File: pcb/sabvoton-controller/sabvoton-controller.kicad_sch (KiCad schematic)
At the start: 26 parts, among them J1 Conn_02x03_Counter_Clockwise, J2 Conn_01x30, U1 ESP32-WROOM-32, U2 XL7015E1, U3 XL7015E1

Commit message: Added 1.8V converter (voltage reference)
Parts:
- added U?: LM1117-1.8, Package_TO_SOT_SMD:SOT-223-3_TabPin2, symbol Regulator_Linear:LM1117-1.8
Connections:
- net 3.3V: now also U?.3 (VI)
- net GND: now also U?.1 (GND)
- new net 1.8V: U?.2 (VO)
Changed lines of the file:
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@@
+    (stroke (width 0) (type default) (color 0 0 0 0))
+  )
+  (wire (pts (xy 572.77 82.55) (xy 579.12 82.55))
     (stroke (width 0) (type default) (color 0 0 0 0))
   )
@@
     (stroke (width 0) (type default) (color 0 0 0 0))
   )
+  (wire (pts (xy 586.74 91.44) (xy 586.74 90.17))
+    (stroke (width 0) (type default) (color 0 0 0 0))
+  )
   (wire (pts (xy 504.19 77.47) (xy 504.19 67.31))
     (stroke (width 0) (type default) (color 0 0 0 0))
   )
+  (wire (pts (xy 571.5 91.44) (xy 586.74 91.44))
+    (stroke (width 0) (type default) (color 0 0 0 0))
+  )
   (wire (pts (xy 506.73 74.93) (xy 511.81 74.93))
     (stroke (width 0) (type default) (color 0 0 0 0))
@@
   )
   (wire (pts (xy 519.43 67.31) (xy 523.24 67.31))
+    (stroke (width 0) (type default) (color 0 0 0 0))
+  )
+  (wire (pts (xy 594.36 82.55) (xy 598.17 82.55))
     (stroke (width 0) (type default) (color 0 0 0 0))
   )
@@
     )
   )
+  (global_label "3.3V" (shape output) (at 572.77 82.55 180) (fields_autoplaced)
+    (effects (font (size 1.27 1.27)) (justify right))
+    (property "Intersheet References" "${INTERSHEET_REFS}" (id 0) (at 566.2445 82.4706 0)
+      (effects (font (size 1.27 1.27)) (justify right) hide)
+    )
+  )
   (global_label "B-" (shape input) (at 436.88 66.04 270) (fields_autoplaced)
     (effects (font (size 1.27 1.27)) (justify right))
@@
     )
   )
+  (global_label "1.8V" (shape input) (at 598.17 82.55 0) (fields_autoplaced)
+    (effects (font (size 1.27 1.27)) (justify left))
+    (property "Intersheet References" "${INTERSHEET_REFS}" (id 0) (at 604.6955 82.4706 0)
+      (effects (font (size 1.27 1.27)) (justify left) hide)
+    )
+  )
   (symbol (lib_id "power:GND") (at 487.68 93.98 0) (unit 1)
     (in_bom yes) (on_board yes) (fields_autoplaced)
@@
     (pin "1")
     (pin "2")
+  )
+  (symbol (lib_id "Regulator_Linear:LM1117-1.8") (at 586.74 82.55 0) (unit 1)
+    (in_bom yes) (on_board yes) (fields_autoplaced)
+    (property "Reference" "U?" (id 0) (at 586.74 74.93 0))
+    (property "Value" "LM1117-1.8" (id 1) (at 586.74 77.47 0))
+    (property "Footprint" "Package_TO_SOT_SMD:SOT-223-3_TabPin2" (id 2) (at 586.74 82.55 0)
+      (effects (font (size 1.27 1.27)) hide)
+    )
+    (property "Datasheet" "http://www.ti.com/lit/ds/symlink/lm1117.pdf" (id 3) (at 586.74 82.55 0)
+      (effects (font (size 1.27 1.27)) hide)
+    )
+    (pin "1")
+    (pin "2")
+    (pin "3")
   )
   (symbol (lib_id "Device:L") (at 516.89 106.68 90) (unit 1)
@@
     (pin "2")
   )
+  (symbol (lib_id "power:GND") (at 571.5 91.44 0) (unit 1)
+    (in_bom yes) (on_board yes) (fields_autoplaced)
+    (property "Reference" "#PWR?" (id 0) (at 571.5 97.79 0)
+      (effects (font (size 1.27 1.27)) hide)
+    )
+    (property "Value" "GND" (id 1) (at 571.5 96.52 0))
+    (property "Footprint" "" (id 2) (at 571.5 91.44 0)
+      (effects (font (size 1.27 1.27)) hide)
+    )
+    (property "Datasheet" "" (id 3) (at 571.5 91.44 0)
+      (effects (font (size 1.27 1.27)) hide)
+    )
+    (pin "1")
+  )
   (symbol (lib_id "Device:C") (at 537.21 71.12 0) (unit 1)
     (in_bom yes) (on_board yes) (fields_autoplaced)
@@
       (reference "#PWR?") (unit 1) (value "GND") (footprint "")
     )
+    (path "/e7b8caad-8c25-46ee-a171-3c952ff2378f"
+      (reference "#PWR?") (unit 1) (value "GND") (footprint "")
+    )
     (path "/d492c89a-b073-4f16-8a2d-e57b90ec8edc"
       (reference "CFF1") (unit 1) (value "C") (footprint "Capacitor_SMD:C_1206_3216Metric_Pad1.33x1.80mm_HandSolder")
@@
       (reference "U3") (unit 1) (value "XL7015E1") (footprint "Package_TO_SOT_SMD:TO-252-5_TabPin3")
     )
+    (path "/4029d2d4-cecc-41e8-82bd-e371ea31d069"
+      (reference "U?") (unit 1) (value "LM1117-1.8") (footprint "Package_TO_SOT_SMD:SOT-223-3_TabPin2")
+    )
     (path "/9a47097d-06a5-4183-845e-85572096854c"

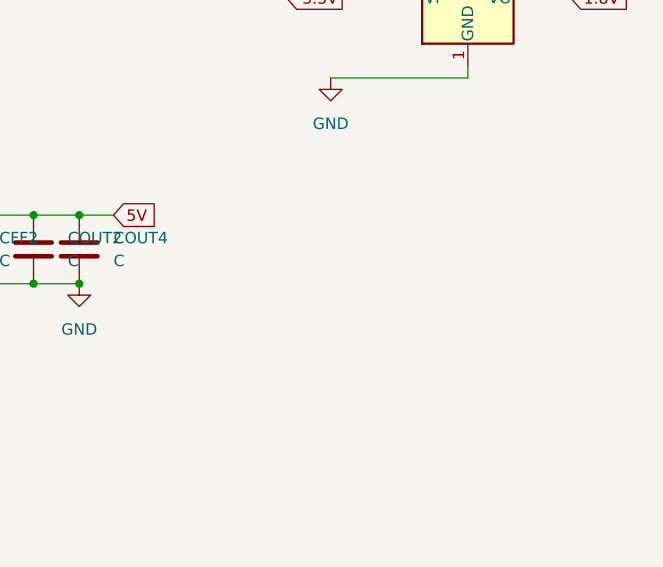
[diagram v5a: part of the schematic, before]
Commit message: Connect negative battery to gnd
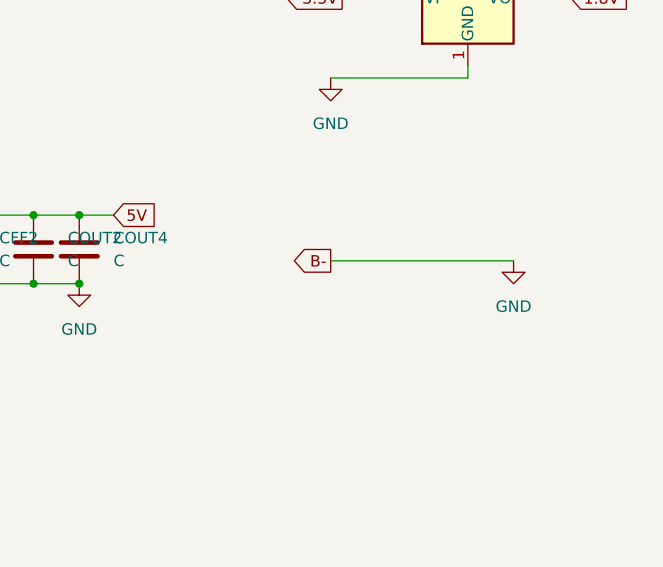
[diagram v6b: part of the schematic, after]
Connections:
- net B- is gone; now on net GND: CIN1.1, CIN2.1, CIN3.1, J2.17 (Pin_17), J2.18 (Pin_18), J2.27 (Pin_27), J2.28 (Pin_28)
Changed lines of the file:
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@@
+    (stroke (width 0) (type default) (color 0 0 0 0))
+  )
+  (wire (pts (xy 571.5 111.76) (xy 591.82 111.76))
     (stroke (width 0) (type default) (color 0 0 0 0))
   )
@@
     )
   )
+  (global_label "B-" (shape output) (at 571.5 111.76 180) (fields_autoplaced)
+    (effects (font (size 1.27 1.27)) (justify right))
+    (property "Intersheet References" "${INTERSHEET_REFS}" (id 0) (at 566.2445 111.6806 0)
+      (effects (font (size 1.27 1.27)) (justify right) hide)
+    )
+  )
   (global_label "3.3V" (shape input) (at 598.17 55.88 0) (fields_autoplaced)
     (effects (font (size 1.27 1.27)) (justify left))
@@
     (pin "1")
     (pin "2")
+  )
+  (symbol (lib_id "power:GND") (at 591.82 111.76 0) (unit 1)
+    (in_bom yes) (on_board yes) (fields_autoplaced)
+    (property "Reference" "#PWR?" (id 0) (at 591.82 118.11 0)
+      (effects (font (size 1.27 1.27)) hide)
+    )
+    (property "Value" "GND" (id 1) (at 591.82 116.84 0))
+    (property "Footprint" "" (id 2) (at 591.82 111.76 0)
+      (effects (font (size 1.27 1.27)) hide)
+    )
+    (property "Datasheet" "" (id 3) (at 591.82 111.76 0)
+      (effects (font (size 1.27 1.27)) hide)
+    )
+    (pin "1")
   )
   (symbol (lib_id "power:GND") (at 542.29 74.93 0) (unit 1)
@@
       (reference "#PWR?") (unit 1) (value "GND") (footprint "")
     )
+    (path "/972aac5e-c9a1-4c35-9267-e07a8dc2778e"
+      (reference "#PWR?") (unit 1) (value "GND") (footprint "")
+    )
